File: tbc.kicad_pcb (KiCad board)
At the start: 2 copper layers, 180 x 67 mm, 118 parts, among them J1 5749181-1, J2 PJRAN1X1U01X, J3 PJRAN1X1U01X, J4 5749181-1, J5 PJRAN1X1U01X, J6 PJRAN3X1U03X, J7 4840.2201, J8 20021111-00010T4LF, Q1 BSS308PE, SW1 1825910-6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

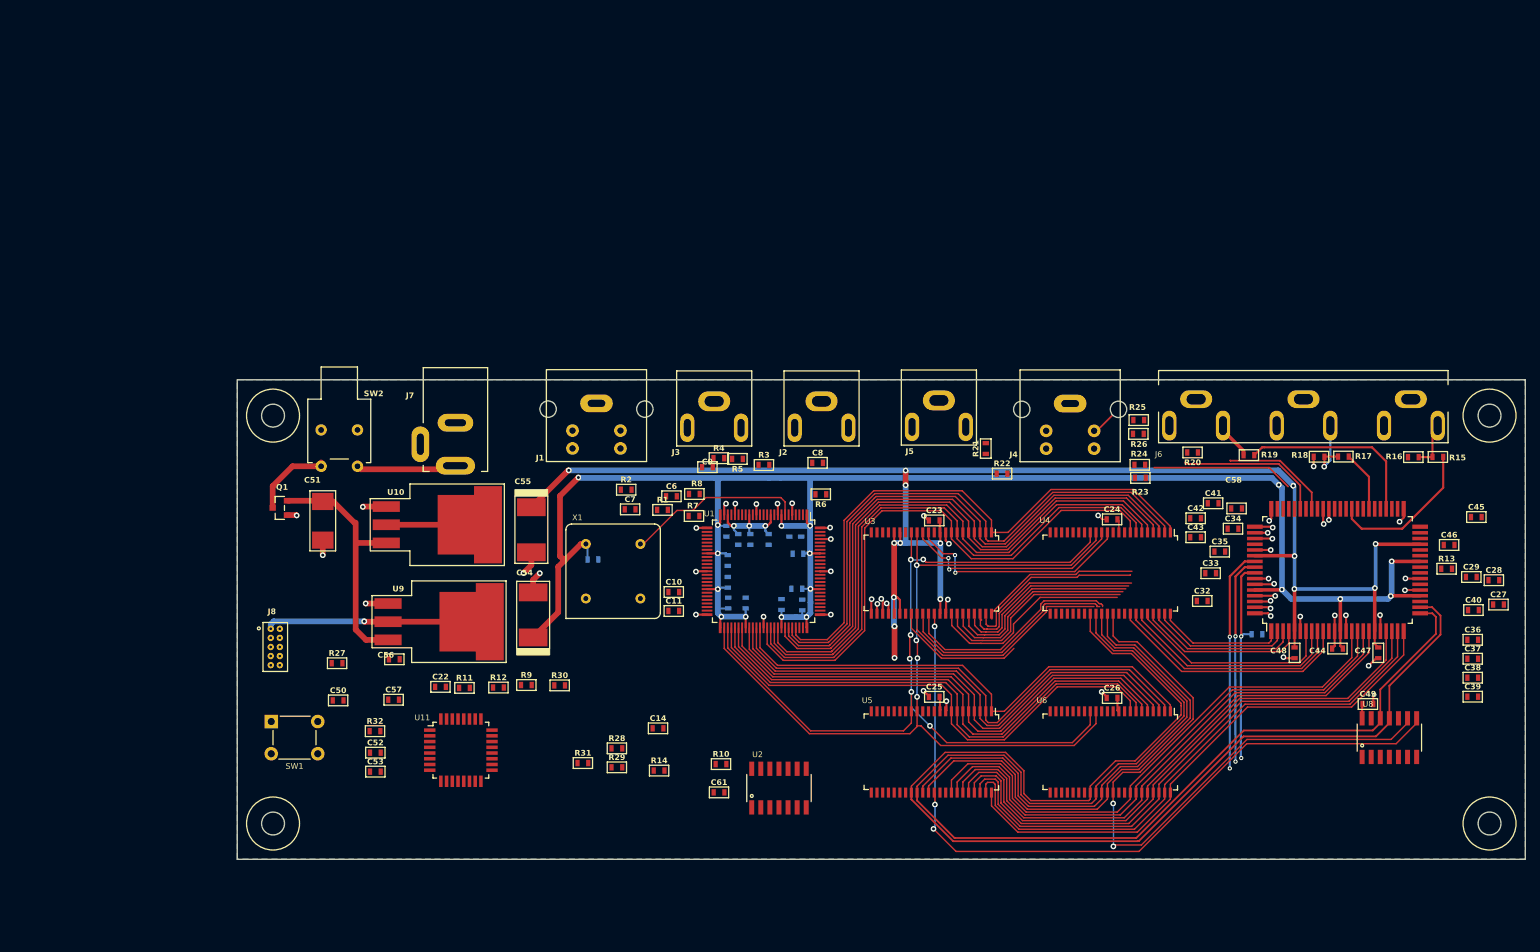
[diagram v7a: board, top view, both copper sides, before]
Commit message: converted to 4-layer pcb
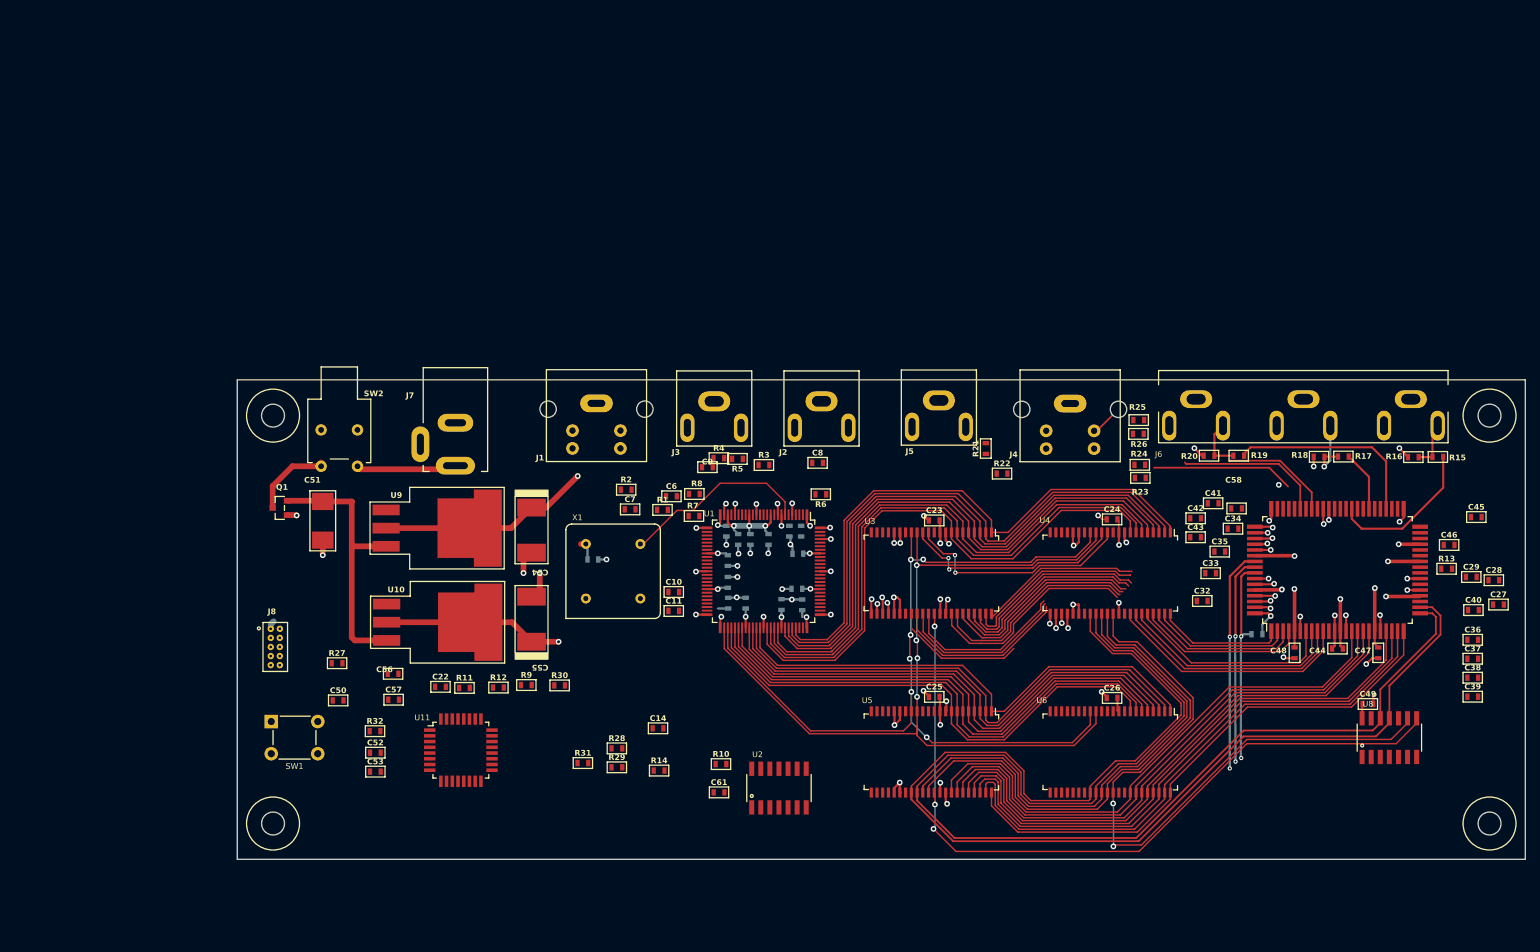
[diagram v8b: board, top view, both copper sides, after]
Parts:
- moved U10 13.6 mm to (100.9, 98.9)
- moved U9 13.1 mm to (100.8, 85.7)
- moved C55 12.5 mm to (121.1, 98.5), turned to 90 degrees
- moved C54 11.9 mm to (121.1, 86.0), turned to -90 degrees
- moved R20 2.34 mm to (215.8, 75.6), turned to 0 degrees
- moved C56 2.03 mm to (101.8, 106.1)
- moved R19 1.43 mm to (219.9, 75.6)
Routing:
- net GND: track 111.4 -> 140.1 mm, vias 54 -> 71
- net +3V3: track 293.7 -> 268.5 mm
- net +5V: track 243.1 -> 226.0 mm, vias 15 -> 18
- net /Frame Memories and Freeze/CREF: track 101.9 -> 93.3 mm
- net /Frame Memories and Freeze/LLC: track 102.5 -> 94.6 mm
- net /Frame Memories and Freeze/RCV1: track 198.5 -> 191.9 mm
- net /Microcontroller, Power/PIN: track 34.7 -> 38.0 mm
- net /Video Encoder/B: track 5.32 -> 8.00 mm
- net Net-(U1-XTALI): track 25.0 -> 26.6 mm
- net Net-(U7-BLUE): track 26.3 -> 27.9 mm
- net /Frame Memories and Freeze/IGPV: track 119.4 -> 120.7 mm
- net /Frame Memories and Freeze/IGPH: track 120.6 -> 121.9 mm
- net /Frame Memories and Freeze/DP7: track 63.2 -> 64.2 mm
- net /Frame Memories and Freeze/DP6: track 61.3 -> 61.9 mm
- added copper zone on In2.Cu, net +5V
- added copper zone on In1.Cu, net GND
- removed copper zone on B.Cu, net GND
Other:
- copper layers 2 -> 4
